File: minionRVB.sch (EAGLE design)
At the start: 106 parts

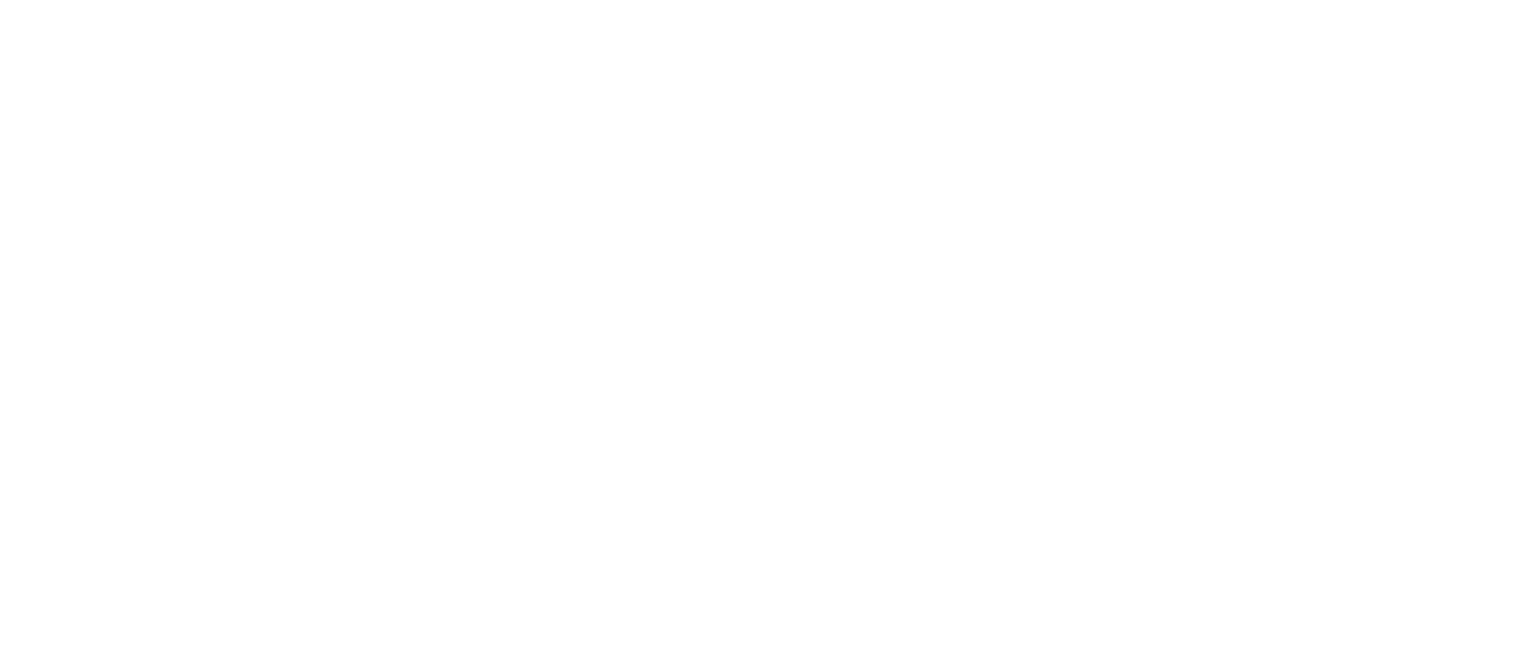
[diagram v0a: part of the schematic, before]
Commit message: Add a teensy adaptor v1
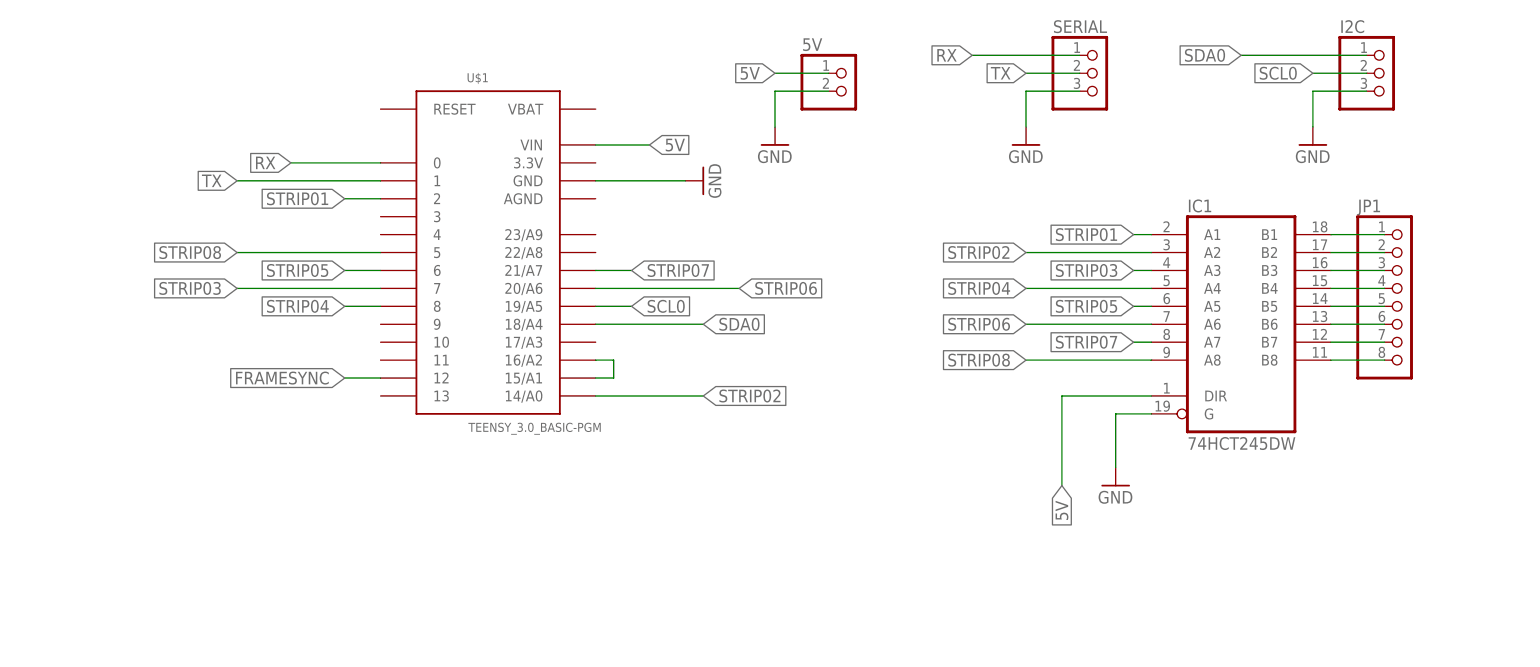
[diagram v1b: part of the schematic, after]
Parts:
- added 5V: (no value), pinhead:PINHD-1X2
- added I2C, SERIAL: (no value), pinhead:PINHD-1X3
- added IC1: 74HCT245DW, 74xx-eu:74HCT245DW
- added JP1: (no value), pinhead:PINHD-1X8
- added U$1: TEENSY_3.0_BASIC-PGM, Teensy3.0:TEENSY_3.0_BASIC-PGM
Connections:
- new net 5V: 5V.1, IC1A.DIR, U$1.VIN
- new net FRAMESYNC: U$1.12
- new net N$1: U$1.15/A1, U$1.16/A2
- new net N$42: IC1A.B1, JP1.1
- new net N$54: IC1A.B2, JP1.2
- new net N$55: IC1A.B3, JP1.3
- new net N$56: IC1A.B4, JP1.4
- new net N$57: IC1A.B5, JP1.5
- new net N$58: IC1A.B6, JP1.6
- new net N$59: IC1A.B7, JP1.7
- new net N$60: IC1A.B8, JP1.8
- new net RX: SERIAL.1, U$1.0
- new net SCL0: I2C.2, U$1.19/A5
- new net SDA0: I2C.1, U$1.18/A4
- new net STRIP01: IC1A.A1, U$1.2
- new net STRIP02: IC1A.A2, U$1.14/A0
- new net STRIP03: IC1A.A3, U$1.7
- new net STRIP04: IC1A.A4, U$1.8
- new net STRIP05: IC1A.A5, U$1.6
- new net STRIP06: IC1A.A6, U$1.20/A6
- new net STRIP07: IC1A.A7, U$1.21/A7
- new net STRIP08: IC1A.A8, U$1.5
- new net TX: SERIAL.2, U$1.1
- net GND: now also 5V.2, I2C.3, IC1A.G, SERIAL.3, U$1.GND

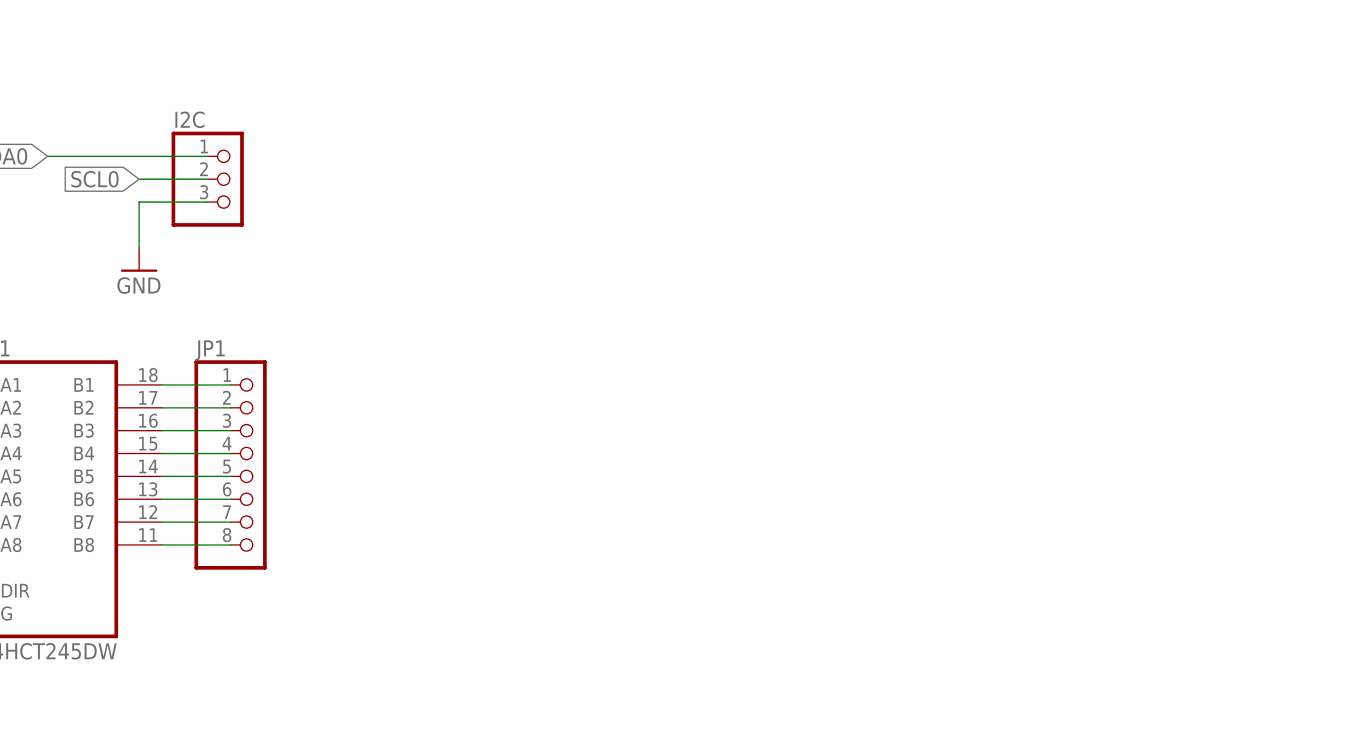
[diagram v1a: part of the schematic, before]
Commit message: Teensy adaptor v2
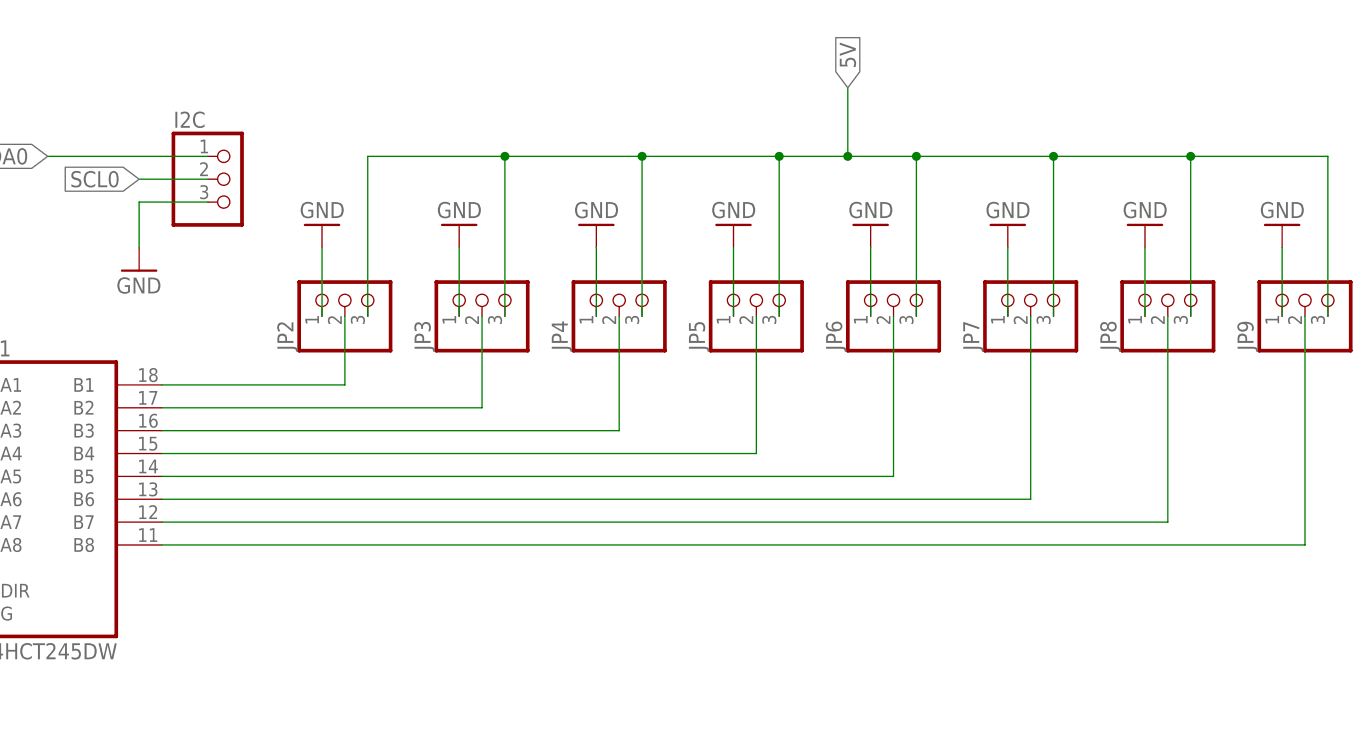
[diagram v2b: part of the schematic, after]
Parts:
- removed JP1: (no value), pinhead:PINHD-1X8
- added JP2, JP3, JP4, JP5, JP6, JP7, JP8, JP9: (no value), pinhead:PINHD-1X3
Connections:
- net 5V: now also JP2.3, JP3.3, JP4.3, JP5.3, JP6.3, JP7.3, JP8.3, JP9.3
- net GND: now also JP2.1, JP3.1, JP4.1, JP5.1, JP6.1, JP7.1, JP8.1, JP9.1
- net N$42: now also JP2.2; no longer JP1.1
- net N$54: now also JP3.2; no longer JP1.2
- net N$55: now also JP4.2; no longer JP1.3
- net N$56: now also JP5.2; no longer JP1.4
- net N$57: now also JP6.2; no longer JP1.5
- net N$58: now also JP7.2; no longer JP1.6
- net N$59: now also JP8.2; no longer JP1.7
- net N$60: now also JP9.2; no longer JP1.8

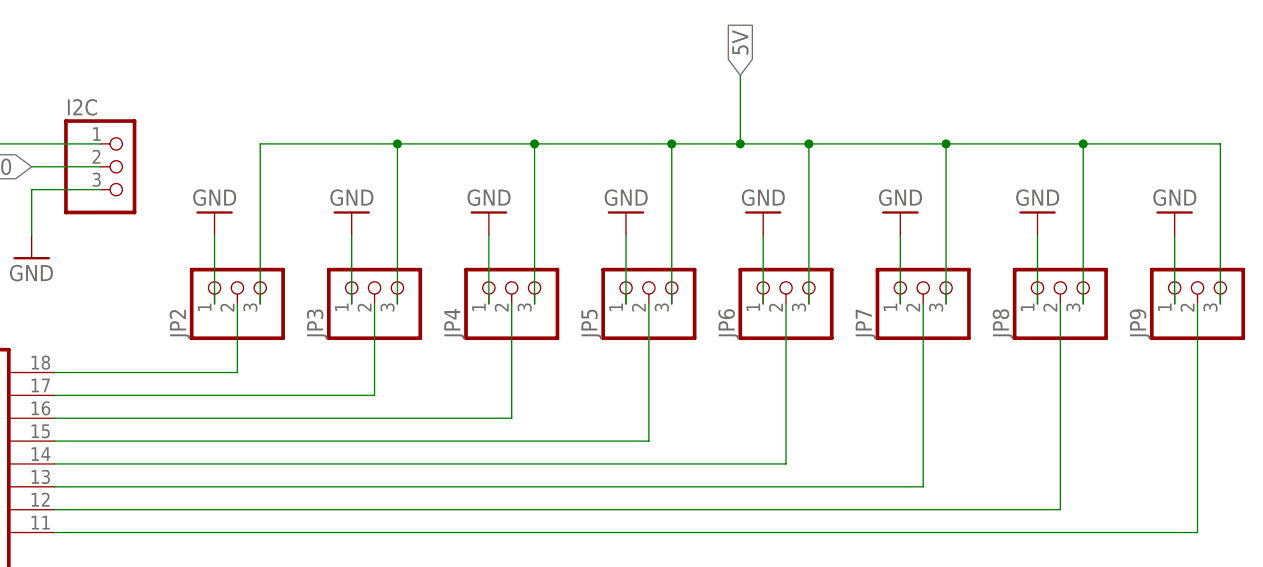
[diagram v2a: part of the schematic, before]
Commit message: Teensy adaptor v3
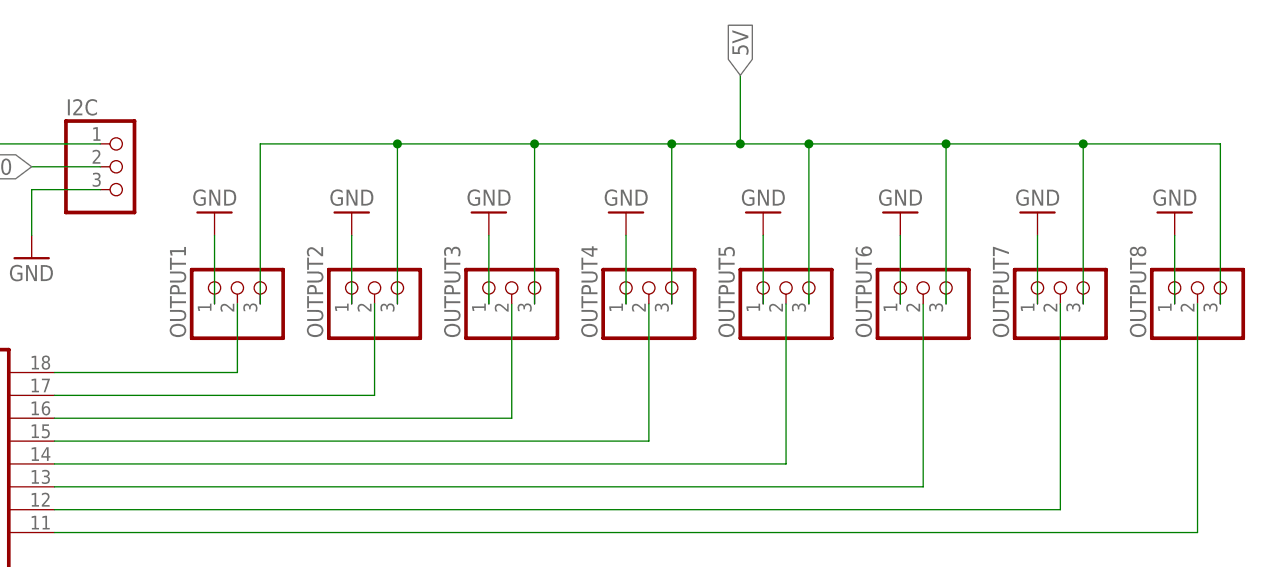
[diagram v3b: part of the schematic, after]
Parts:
- renumbered JP2 to OUTPUT1, JP3 to OUTPUT2, JP4 to OUTPUT3, JP5 to OUTPUT4, JP6 to OUTPUT5, JP7 to OUTPUT6, JP8 to OUTPUT7, JP9 to OUTPUT8
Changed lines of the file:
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@@
 <part name="5V" library="pinhead" deviceset="PINHD-1X2" device=""/>
 <part name="GND111" library="SparkFun" deviceset="GND" device=""/>
-<part name="JP2" library="pinhead" deviceset="PINHD-1X3" device=""/>
-<part name="JP3" library="pinhead" deviceset="PINHD-1X3" device=""/>
-<part name="JP4" library="pinhead" deviceset="PINHD-1X3" device=""/>
-<part name="JP5" library="pinhead" deviceset="PINHD-1X3" device=""/>
-<part name="JP6" library="pinhead" deviceset="PINHD-1X3" device=""/>
-<part name="JP7" library="pinhead" deviceset="PINHD-1X3" device=""/>
-<part name="JP8" library="pinhead" deviceset="PINHD-1X3" device=""/>
-<part name="JP9" library="pinhead" deviceset="PINHD-1X3" device=""/>
+<part name="OUTPUT1" library="pinhead" deviceset="PINHD-1X3" device=""/>
+<part name="OUTPUT2" library="pinhead" deviceset="PINHD-1X3" device=""/>
+<part name="OUTPUT3" library="pinhead" deviceset="PINHD-1X3" device=""/>
+<part name="OUTPUT4" library="pinhead" deviceset="PINHD-1X3" device=""/>
+<part name="OUTPUT5" library="pinhead" deviceset="PINHD-1X3" device=""/>
+<part name="OUTPUT6" library="pinhead" deviceset="PINHD-1X3" device=""/>
+<part name="OUTPUT7" library="pinhead" deviceset="PINHD-1X3" device=""/>
+<part name="OUTPUT8" library="pinhead" deviceset="PINHD-1X3" device=""/>
 <part name="GND112" library="SparkFun" deviceset="GND" device=""/>
 <part name="GND113" library="SparkFun" deviceset="GND" device=""/>
@@
 <instance part="5V" gate="G$1" x="386.08" y="215.9"/>
 <instance part="GND111" gate="1" x="375.92" y="208.28"/>
-<instance part="JP2" gate="A" x="474.98" y="205.74" rot="R90"/>
-<instance part="JP3" gate="A" x="490.22" y="205.74" rot="R90"/>
-<instance part="JP4" gate="A" x="505.46" y="205.74" rot="R90"/>
-<instance part="JP5" gate="A" x="520.7" y="205.74" rot="R90"/>
-<instance part="JP6" gate="A" x="535.94" y="205.74" rot="R90"/>
-<instance part="JP7" gate="A" x="551.18" y="205.74" rot="R90"/>
-<instance part="JP8" gate="A" x="566.42" y="205.74" rot="R90"/>
-<instance part="JP9" gate="A" x="581.66" y="205.74" rot="R90"/>
+<instance part="OUTPUT1" gate="A" x="474.98" y="205.74" rot="R90"/>
+<instance part="OUTPUT2" gate="A" x="490.22" y="205.74" rot="R90"/>
+<instance part="OUTPUT3" gate="A" x="505.46" y="205.74" rot="R90"/>
+<instance part="OUTPUT4" gate="A" x="520.7" y="205.74" rot="R90"/>
+<instance part="OUTPUT5" gate="A" x="535.94" y="205.74" rot="R90"/>
+<instance part="OUTPUT6" gate="A" x="551.18" y="205.74" rot="R90"/>
+<instance part="OUTPUT7" gate="A" x="566.42" y="205.74" rot="R90"/>
+<instance part="OUTPUT8" gate="A" x="581.66" y="205.74" rot="R90"/>
 <instance part="GND112" gate="1" x="533.4" y="213.36" rot="R180"/>
 <instance part="GND113" gate="1" x="487.68" y="213.36" rot="R180"/>
@@
 </segment>
 <segment>
-<pinref part="JP3" gate="A" pin="1"/>
+<pinref part="OUTPUT2" gate="A" pin="1"/>
 <wire x1="487.68" y1="203.2" x2="487.68" y2="210.82" width="0.1524" layer="91"/>
 <pinref part="GND113" gate="1" pin="GND"/>
 </segment>
 <segment>
-<pinref part="JP2" gate="A" pin="1"/>
+<pinref part="OUTPUT1" gate="A" pin="1"/>
 <wire x1="472.44" y1="203.2" x2="472.44" y2="210.82" width="0.1524" layer="91"/>
 <pinref part="GND114" gate="1" pin="GND"/>
 </segment>
 <segment>
-<pinref part="JP4" gate="A" pin="1"/>
+<pinref part="OUTPUT3" gate="A" pin="1"/>
 <wire x1="502.92" y1="203.2" x2="502.92" y2="210.82" width="0.1524" layer="91"/>
 <pinref part="GND115" gate="1" pin="GND"/>
 </segment>
 <segment>
-<pinref part="JP5" gate="A" pin="1"/>
+<pinref part="OUTPUT4" gate="A" pin="1"/>
 <wire x1="518.16" y1="203.2" x2="518.16" y2="210.82" width="0.1524" layer="91"/>
 <pinref part="GND116" gate="1" pin="GND"/>
 </segment>
 <segment>
-<pinref part="JP6" gate="A" pin="1"/>
+<pinref part="OUTPUT5" gate="A" pin="1"/>
 <wire x1="533.4" y1="203.2" x2="533.4" y2="210.82" width="0.1524" layer="91"/>
 <pinref part="GND112" gate="1" pin="GND"/>
 </segment>
 <segment>
-<pinref part="JP7" gate="A" pin="1"/>
+<pinref part="OUTPUT6" gate="A" pin="1"/>
 <wire x1="548.64" y1="203.2" x2="548.64" y2="210.82" width="0.1524" layer="91"/>
 <pinref part="GND117" gate="1" pin="GND"/>
 </segment>
 <segment>
-<pinref part="JP8" gate="A" pin="1"/>
+<pinref part="OUTPUT7" gate="A" pin="1"/>
 <wire x1="563.88" y1="203.2" x2="563.88" y2="210.82" width="0.1524" layer="91"/>
 <pinref part="GND118" gate="1" pin="GND"/>
 </segment>
 <segment>
-<pinref part="JP9" gate="A" pin="1"/>
+<pinref part="OUTPUT8" gate="A" pin="1"/>
 <wire x1="579.12" y1="203.2" x2="579.12" y2="210.82" width="0.1524" layer="91"/>
 <pinref part="GND119" gate="1" pin="GND"/>
@@
 <segment>
 <pinref part="IC1" gate="A" pin="B1"/>
-<pinref part="JP2" gate="A" pin="2"/>
+<pinref part="OUTPUT1" gate="A" pin="2"/>
 <wire x1="454.66" y1="195.58" x2="474.98" y2="195.58" width="0.1524" layer="91"/>
 <wire x1="474.98" y1="195.58" x2="474.98" y2="203.2" width="0.1524" layer="91"/>
@@
 <segment>
 <pinref part="IC1" gate="A" pin="B2"/>
-<pinref part="JP3" gate="A" pin="2"/>
+<pinref part="OUTPUT2" gate="A" pin="2"/>
 <wire x1="454.66" y1="193.04" x2="490.22" y2="193.04" width="0.1524" layer="91"/>
 <wire x1="490.22" y1="193.04" x2="490.22" y2="203.2" width="0.1524" layer="91"/>
@@
 <segment>
 <pinref part="IC1" gate="A" pin="B3"/>
-<pinref part="JP4" gate="A" pin="2"/>
+<pinref part="OUTPUT3" gate="A" pin="2"/>
 <wire x1="454.66" y1="190.5" x2="505.46" y2="190.5" width="0.1524" layer="91"/>
 <wire x1="505.46" y1="190.5" x2="505.46" y2="203.2" width="0.1524" layer="91"/>
@@
 <segment>
 <pinref part="IC1" gate="A" pin="B4"/>
-<pinref part="JP5" gate="A" pin="2"/>
+<pinref part="OUTPUT4" gate="A" pin="2"/>
 <wire x1="454.66" y1="187.96" x2="520.7" y2="187.96" width="0.1524" layer="91"/>
 <wire x1="520.7" y1="187.96" x2="520.7" y2="203.2" width="0.1524" layer="91"/>
@@
 <segment>
 <pinref part="IC1" gate="A" pin="B5"/>
-<pinref part="JP6" gate="A" pin="2"/>
+<pinref part="OUTPUT5" gate="A" pin="2"/>
 <wire x1="454.66" y1="185.42" x2="535.94" y2="185.42" width="0.1524" layer="91"/>
 <wire x1="535.94" y1="185.42" x2="535.94" y2="203.2" width="0.1524" layer="91"/>
@@
 <segment>
 <pinref part="IC1" gate="A" pin="B6"/>
-<pinref part="JP7" gate="A" pin="2"/>
+<pinref part="OUTPUT6" gate="A" pin="2"/>
 <wire x1="454.66" y1="182.88" x2="551.18" y2="182.88" width="0.1524" layer="91"/>
 <wire x1="551.18" y1="182.88" x2="551.18" y2="203.2" width="0.1524" layer="91"/>
@@
 <segment>
 <pinref part="IC1" gate="A" pin="B7"/>
-<pinref part="JP8" gate="A" pin="2"/>
+<pinref part="OUTPUT7" gate="A" pin="2"/>
 <wire x1="454.66" y1="180.34" x2="566.42" y2="180.34" width="0.1524" layer="91"/>
 <wire x1="566.42" y1="180.34" x2="566.42" y2="203.2" width="0.1524" layer="91"/>
@@
 <segment>
 <pinref part="IC1" gate="A" pin="B8"/>
-<pinref part="JP9" gate="A" pin="2"/>
+<pinref part="OUTPUT8" gate="A" pin="2"/>
 <wire x1="454.66" y1="177.8" x2="581.66" y2="177.8" width="0.1524" layer="91"/>
 <wire x1="581.66" y1="177.8" x2="581.66" y2="203.2" width="0.1524" layer="91"/>
@@
 </segment>
 <segment>
-<pinref part="JP2" gate="A" pin="3"/>
+<pinref part="OUTPUT1" gate="A" pin="3"/>
 <wire x1="477.52" y1="203.2" x2="477.52" y2="220.98" width="0.1524" layer="91"/>
-<pinref part="JP3" gate="A" pin="3"/>
+<pinref part="OUTPUT2" gate="A" pin="3"/>
 <wire x1="477.52" y1="220.98" x2="492.76" y2="220.98" width="0.1524" layer="91"/>
 <wire x1="492.76" y1="220.98" x2="492.76" y2="203.2" width="0.1524" layer="91"/>
-<pinref part="JP4" gate="A" pin="3"/>
+<pinref part="OUTPUT3" gate="A" pin="3"/>
 <wire x1="492.76" y1="220.98" x2="508" y2="220.98" width="0.1524" layer="91"/>
 <wire x1="508" y1="220.98" x2="508" y2="203.2" width="0.1524" layer="91"/>
 <junction x="492.76" y="220.98"/>
-<pinref part="JP5" gate="A" pin="3"/>
+<pinref part="OUTPUT4" gate="A" pin="3"/>
 <wire x1="508" y1="220.98" x2="523.24" y2="220.98" width="0.1524" layer="91"/>
 <wire x1="523.24" y1="220.98" x2="523.24" y2="203.2" width="0.1524" layer="91"/>
 <junction x="508" y="220.98"/>
-<pinref part="JP6" gate="A" pin="3"/>
+<pinref part="OUTPUT5" gate="A" pin="3"/>
 <wire x1="523.24" y1="220.98" x2="530.86" y2="220.98" width="0.1524" layer="91"/>
 <wire x1="530.86" y1="220.98" x2="538.48" y2="220.98" width="0.1524" layer="91"/>
 <wire x1="538.48" y1="220.98" x2="538.48" y2="203.2" width="0.1524" layer="91"/>
 <junction x="523.24" y="220.98"/>
-<pinref part="JP7" gate="A" pin="3"/>
+<pinref part="OUTPUT6" gate="A" pin="3"/>
 <wire x1="538.48" y1="220.98" x2="553.72" y2="220.98" width="0.1524" layer="91"/>
 <wire x1="553.72" y1="220.98" x2="553.72" y2="203.2" width="0.1524" layer="91"/>
 <junction x="538.48" y="220.98"/>
-<pinref part="JP8" gate="A" pin="3"/>
+<pinref part="OUTPUT7" gate="A" pin="3"/>
 <wire x1="553.72" y1="220.98" x2="568.96" y2="220.98" width="0.1524" layer="91"/>
 <wire x1="568.96" y1="220.98" x2="568.96" y2="203.2" width="0.1524" layer="91"/>
 <junction x="553.72" y="220.98"/>
-<pinref part="JP9" gate="A" pin="3"/>
+<pinref part="OUTPUT8" gate="A" pin="3"/>
 <wire x1="568.96" y1="220.98" x2="584.2" y2="220.98" width="0.1524" layer="91"/>
 <wire x1="584.2" y1="220.98" x2="584.2" y2="203.2" width="0.1524" layer="91"/>
